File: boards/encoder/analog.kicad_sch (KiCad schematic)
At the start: 29 parts, among them Q1 NPN, Q2 PNP, Q3 NMOS, U3 LMR342, U4 CT310, U5 INA826, U6 INA826, U7 AZ431-A, U8 Opamp_Dual, U9 LMR342

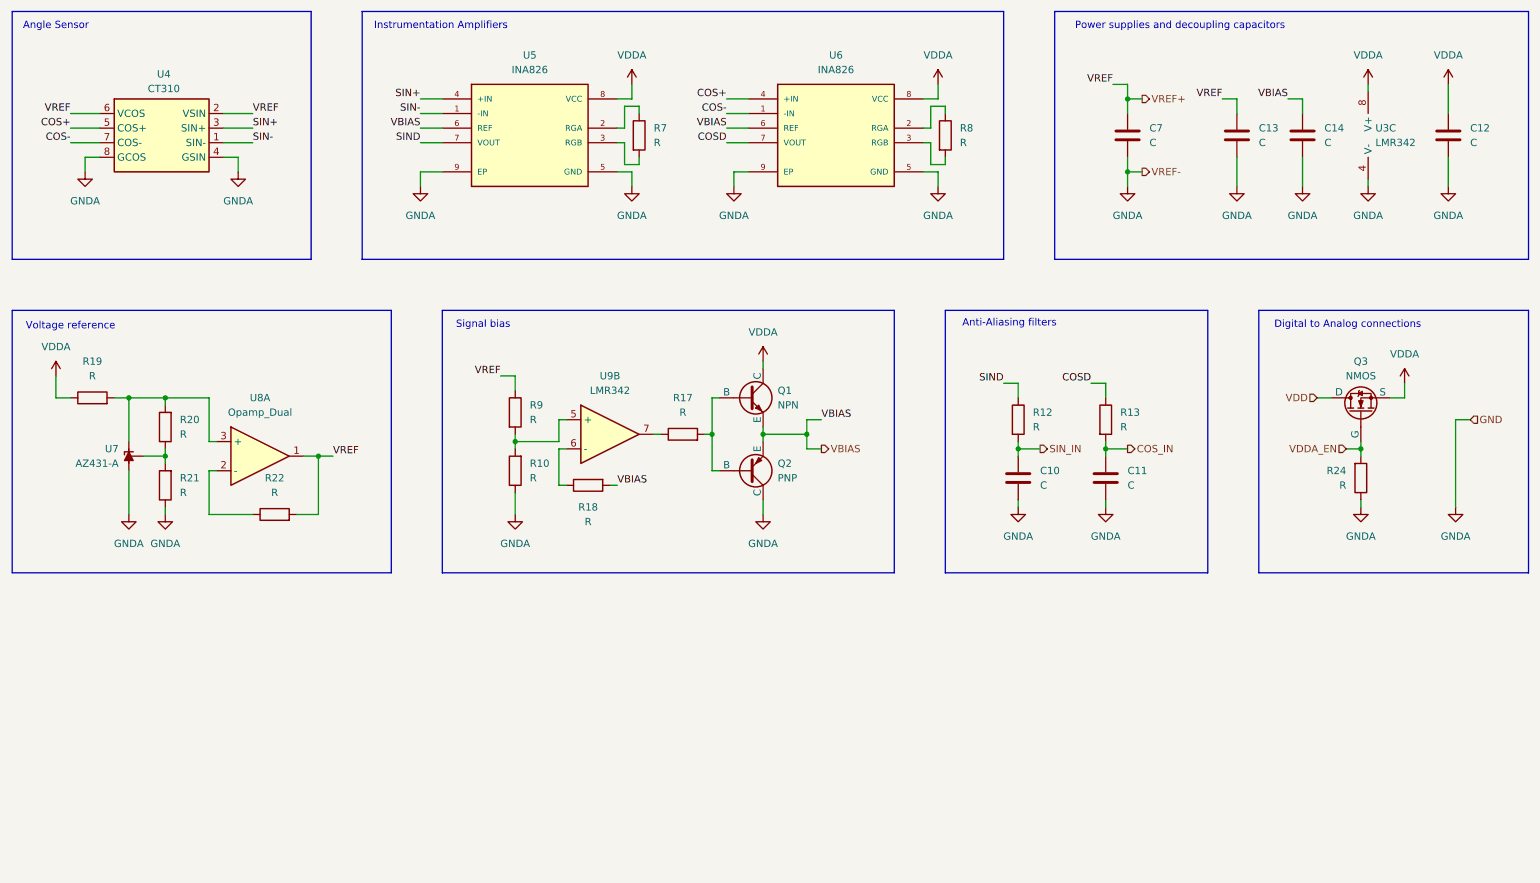
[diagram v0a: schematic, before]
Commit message: Added second decoupling capacitor
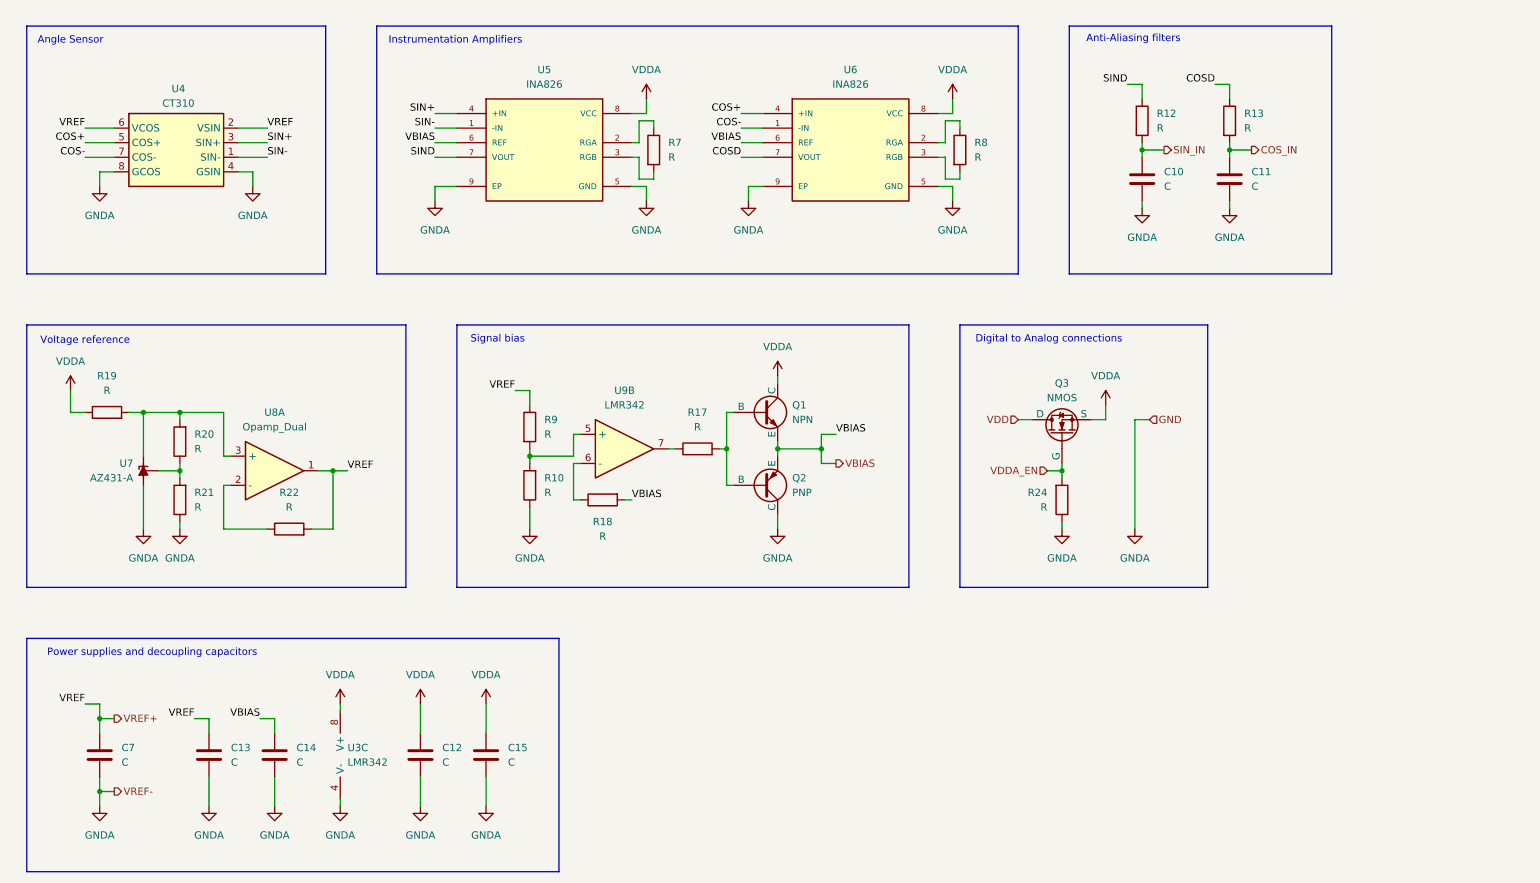
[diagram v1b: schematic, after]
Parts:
- added C15: C, symbol Device:C
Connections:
- net GNDA: now also C15.2
- net VDDA: now also C15.1
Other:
- moved on the sheet: C10, C11, C12, C13, C14, C7, Q1, Q2, Q3, R10, R12, R13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

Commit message: Moved busses to external sheet
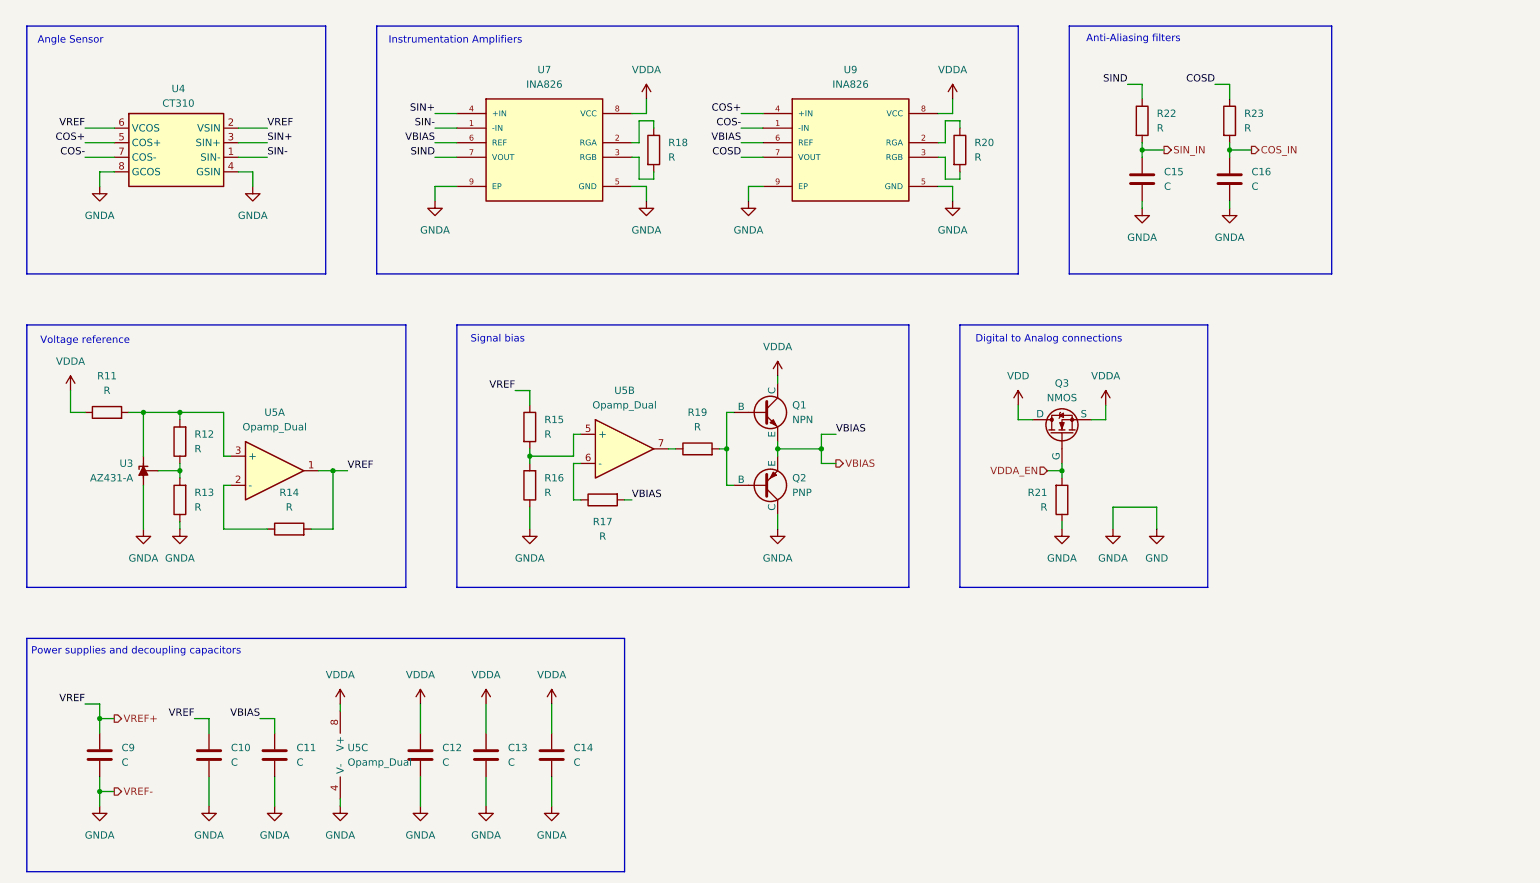
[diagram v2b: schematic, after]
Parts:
- removed U3, U9: LMR342, symbol Device:Opamp_Dual
- removed U8: Opamp_Dual, symbol Device:Opamp_Dual
- added C14: C, symbol Device:C
- added U5: Opamp_Dual, symbol Device:Opamp_Dual
- renumbered C13 to C10, C14 to C11, C15 to C13, C10 to C15, C11 to C16, C7 to C9, R19 to R11, R20 to R12, R21 to R13, R22 to R14, R9 to R15, R10 to R16, R18 to R17, R7 to R18, R17 to R19, R8 to R20, R24 to R21, R12 to R22, R13 to R23, U7 to U3, U5 to U7, U6 to U9
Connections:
- net VDDA: now also C14.1, U5.8 (V+)
- net VREF+: now also U5.1
- net at R15.2, R16.2: now also U5.5 (+)
- net at R11.2, R12.2, U3.1 (K): now also U5.3 (+)
- net at R14.1: now also U5.2 (-)
- net at R17.1: now also U5.6 (-)
- net at R19.1: now also U5.7
- net GNDA renamed GND
- net GND: now also C14.2, U5.4 (V-)
